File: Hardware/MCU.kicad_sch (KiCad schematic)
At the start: 27 parts, among them J6 USART Breakout, J7 SWD, SW1 Reset, U3 STM32L431CBTx, Y1 8M

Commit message: organization, updated submodule
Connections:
- net LED_FAULT: now reaches R13.1
- net LED_FAULT: now also U3.14 (PA4)
- net LED_CHARGE: now reaches R14.1
- net LED_CHARGE: now also U3.15 (PA5)
- net LED_DISCHARGE: now reaches R15.1
- net LED_DISCHARGE: now also U3.16 (PA6)
- net LED_HB: now reaches U3.13 (PA3)
- net LED_HB: now also R12.1
- net PA0 renamed ADC1_IN5
- net ADC1_IN5: no longer R12.1
- net PA1: no longer names the net of U3.11 (PA1)
- no-connect marks 27 -> 24
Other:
- note added: "LED Indicators"
- note removed: "Keep terminating resistors close to the pins Make sure to put resistor at MISO at the other end"
- note removed: "LEDs"
- moved on the sheet: C10, C11, C12, C7, C8, C9

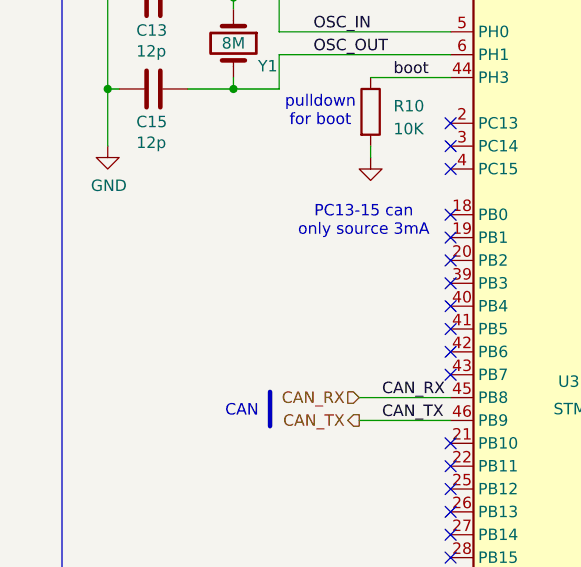
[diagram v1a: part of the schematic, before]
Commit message: new isolated amp, filter stage; need to select values
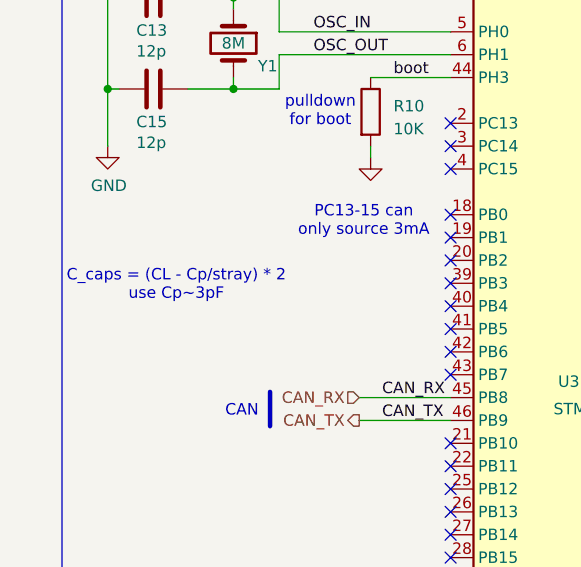
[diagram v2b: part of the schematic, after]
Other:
- note added: "C_caps = (CL - Cp/stray) * 2 use Cp~3pF"
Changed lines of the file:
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@@
+		)
+	)
+	(text "C_caps = (CL - Cp/stray) * 2\nuse Cp~3pF"
+		(exclude_from_sim no)
+		(at 27.94 68.834 0)
+		(effects
+			(font
+				(size 1.27 1.27)
+			)
 		)
 	)

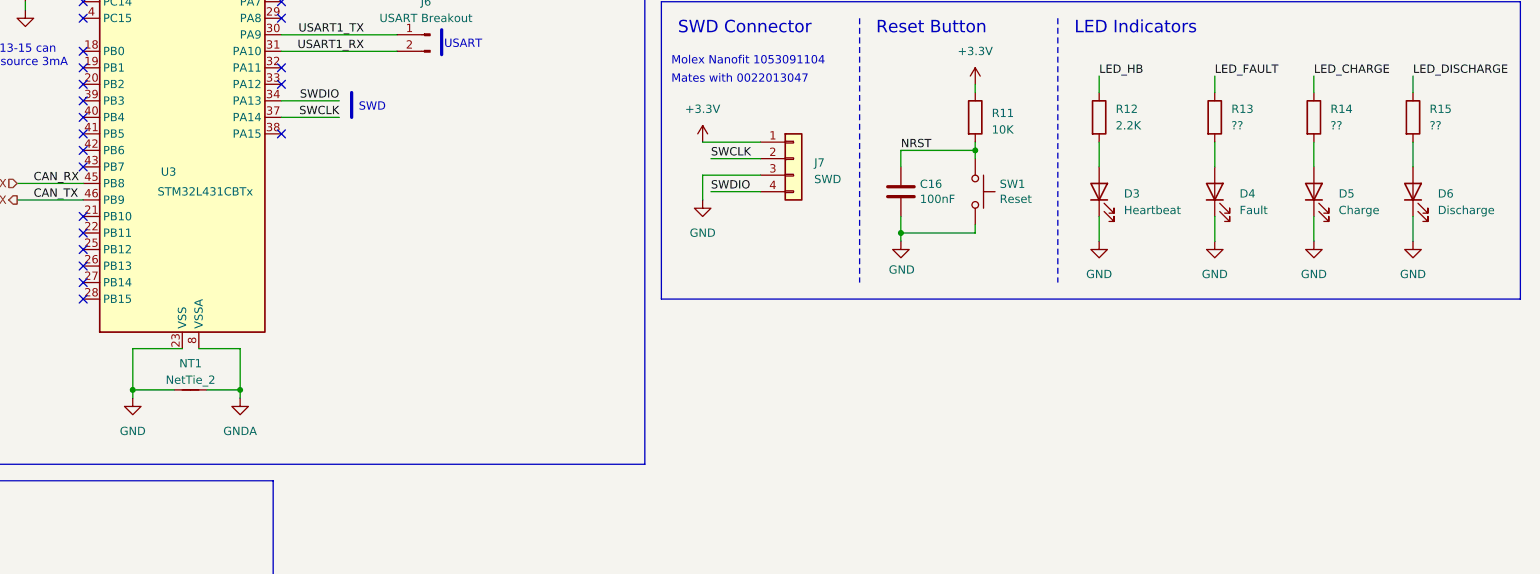
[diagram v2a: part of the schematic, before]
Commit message: added LEDs, changed LDO, still need to address other comments
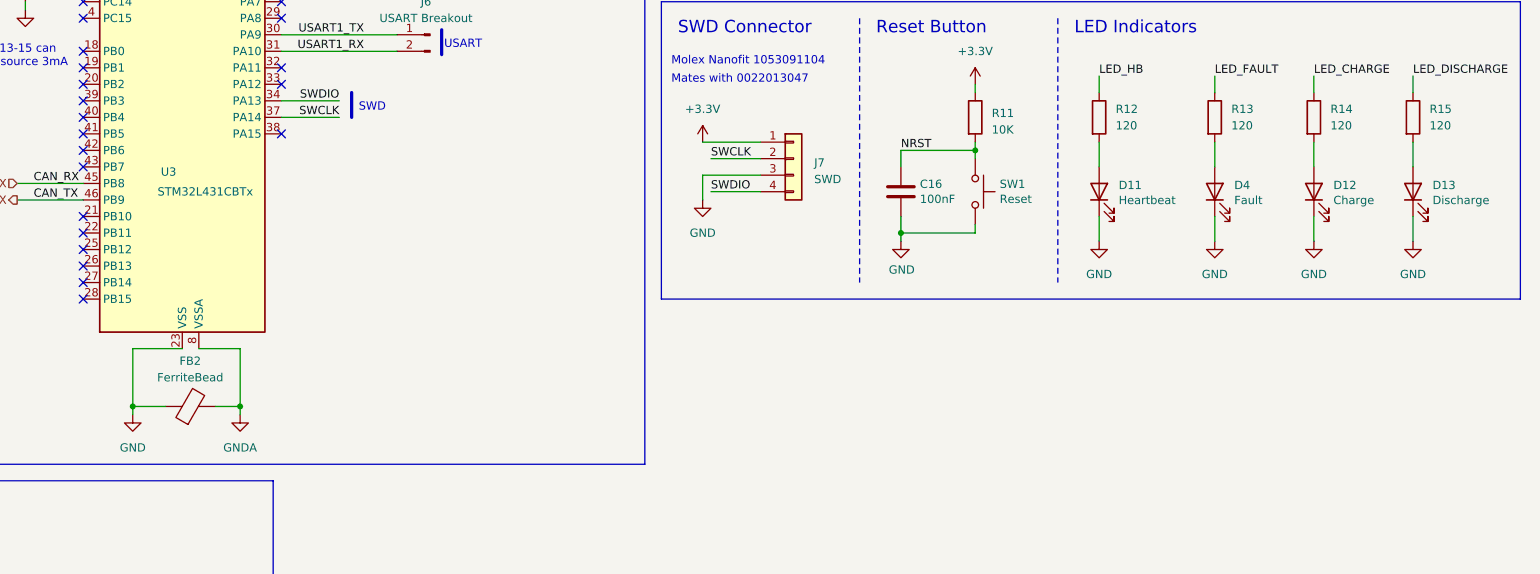
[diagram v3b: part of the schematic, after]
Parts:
- removed D3: Heartbeat, LED_SMD:LED_0805_2012Metric, symbol Device:LED
- removed D5: Charge, LED_SMD:LED_0805_2012Metric, symbol Device:LED
- removed D6: Discharge, LED_SMD:LED_0805_2012Metric, symbol Device:LED
- removed NT1: NetTie_2, NetTie:NetTie-2_SMD_Pad0.5mm, symbol Device:NetTie_2
- added D11: Heartbeat, symbol Device:LED
- added D12: Charge, symbol Device:LED
- added D13: Discharge, symbol Device:LED
- added FB2: FerriteBead, Inductor_SMD:L_0805_2012Metric, symbol Device:FerriteBead
- D4: footprint LED_SMD:LED_0805_2012Metric -> (none); Mfg (none) -> NCD0603R1
- R12: value 2.2K -> 120
- R13, R14, R15: value ?? -> 120
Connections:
- net GND: now also D11.1 (K), D12.1 (K), D13.1 (K), FB2.1
- net GNDA: now also FB2.2
- net at R14.2: now also D12.2 (A)
- net at R15.2: now also D13.2 (A)
- net at R12.2: now also D11.2 (A)

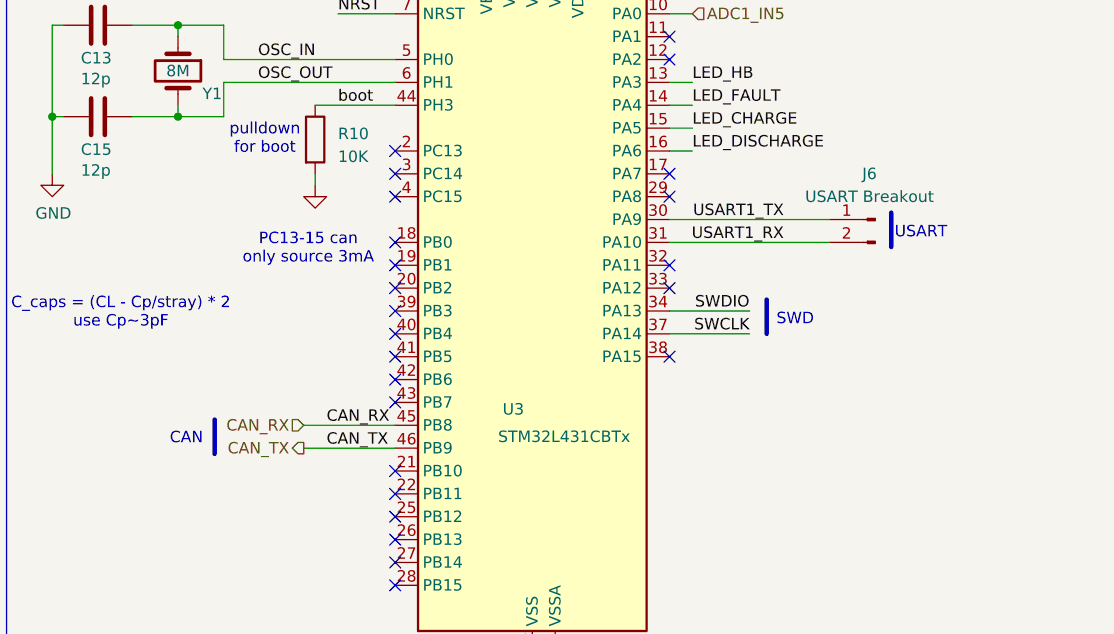
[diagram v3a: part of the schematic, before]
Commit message: scrutineering should be done, started on USB
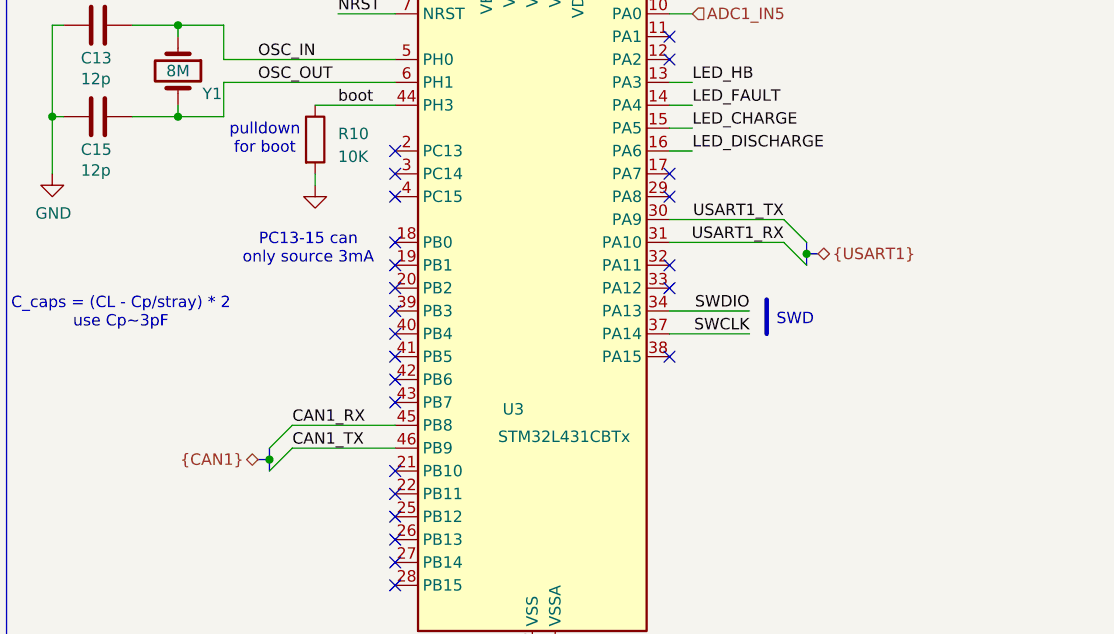
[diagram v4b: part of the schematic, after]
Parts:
- removed J6: USART Breakout, Connector_PinHeader_2.54mm:PinHeader_1x02_P2.54mm_Vertical, symbol Connector:Conn_01x02_Pin
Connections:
- net CAN_RX renamed CAN1_RX
- net CAN_TX renamed CAN1_TX
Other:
- note removed: "CAN"
- note removed: "USART"

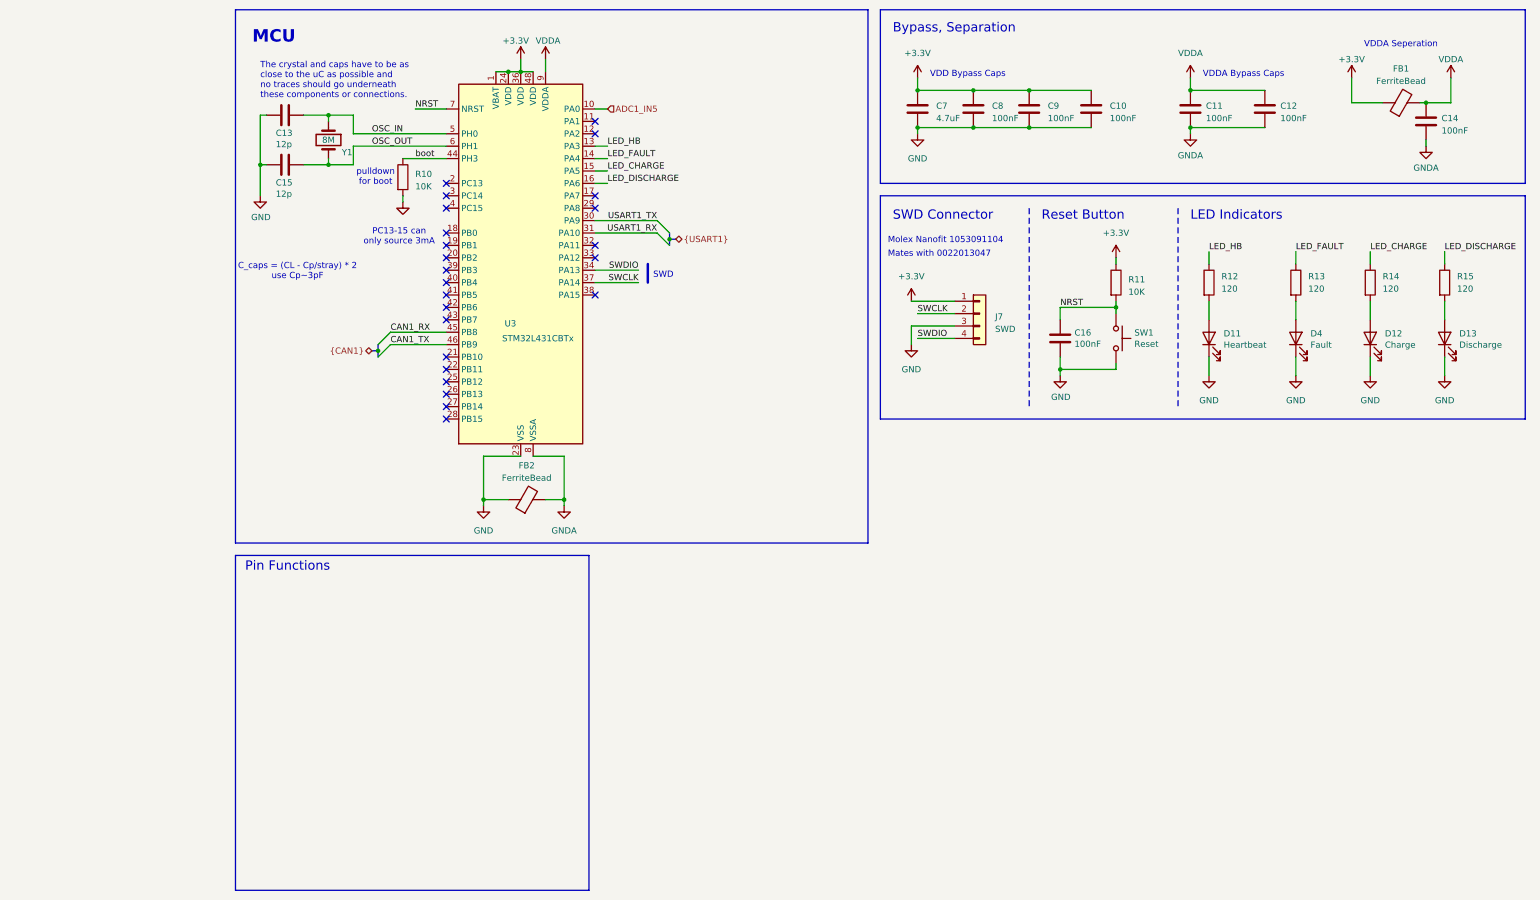
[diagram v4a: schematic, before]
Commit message: copied USB-C from psom
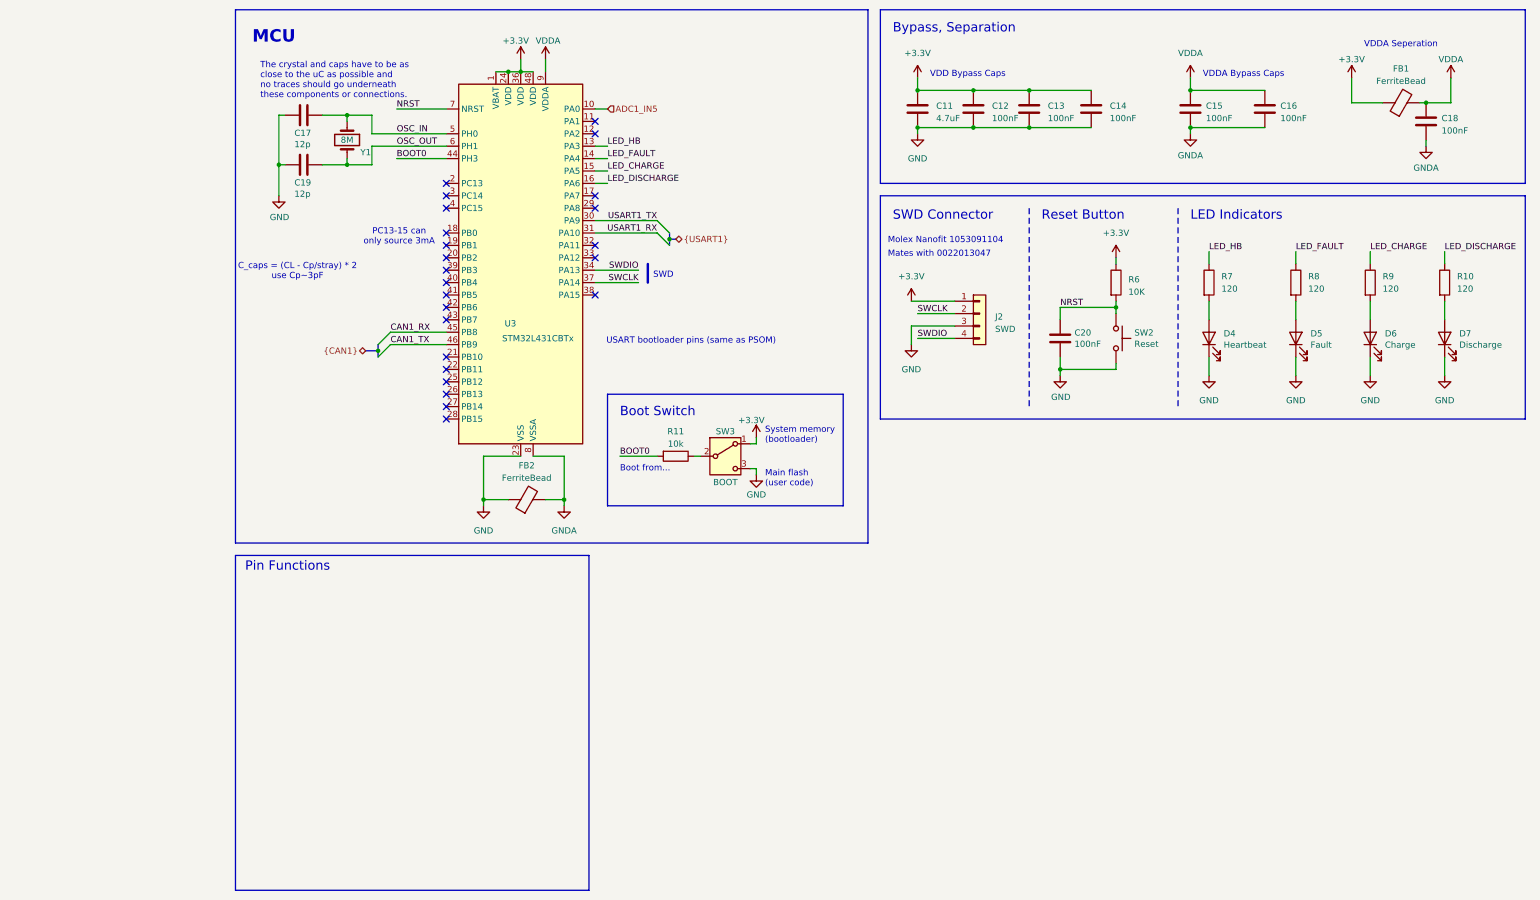
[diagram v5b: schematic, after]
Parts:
- removed R10: 10K, Resistor_SMD:R_0805_2012Metric, symbol Device:R
- added R11: 10k, Resistor_SMD:R_0603_1608Metric_Pad0.98x0.95mm_HandSolder, symbol Device:R
- added SW3: BOOT, CJS-1200TA:SW_CJS-1200TA, symbol Switch:SW_SPDT
- renumbered C7 to C11, C8 to C12, C9 to C13, C10 to C14, C11 to C15, C12 to C16, C13 to C17, C14 to C18, C15 to C19, C16 to C20, D11 to D4, D4 to D5, D12 to D6, D13 to D7, J7 to J2, R15 to R10, R11 to R6, R12 to R7, R13 to R8, R14 to R9, SW1 to SW2
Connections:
- net +3.3V: now also SW3.1 (A)
- net GND: now also SW3.3 (C)
- net boot renamed BOOT0
- net BOOT0: now also R11.2
- new net: R11.1, SW3.2 (B)
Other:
- note added: "Boot Switch"
- note added: "Boot from..."
- note added: "Main flash (user code)"
- note added: "System memory (bootloader)"
- note added: "USART bootloader pins (same as PSOM)"
- note removed: "pulldown for boot"
- moved on the sheet: C17, C19, Y1

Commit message: something changed idk what though
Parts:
- renumbered C11 to C18, C12 to C19, C13 to C20, C14 to C21, C15 to C22, C16 to C23, C17 to C24, C18 to C25, C19 to C26, C20 to C27, D4 to D6, D5 to D7, D6 to D8, D7 to D9, J2 to J3, R6 to R11, R7 to R12, R8 to R13, R9 to R14, R10 to R15, R11 to R16, U3 to U4

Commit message: 0603 footprints
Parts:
- C18, C19, C20, C21, C22, C23, C24, C25, C26, C27: footprint Capacitor_SMD:C_0805_2012Metric -> Capacitor_SMD:C_0603_1608Metric_Pad1.08x0.95mm_HandSolder
- D6, D7, D8, D9: footprint (none) -> LED_SMD:LED_0603_1608Metric_Pad1.05x0.95mm_HandSolder
- FB1, FB2: footprint Inductor_SMD:L_0805_2012Metric -> Capacitor_SMD:C_0603_1608Metric_Pad1.08x0.95mm_HandSolder
- R11, R12, R13, R14, R15: footprint Resistor_SMD:R_0805_2012Metric -> Resistor_SMD:R_0603_1608Metric_Pad0.98x0.95mm_HandSolder
- SW3: footprint CJS-1200TA:SW_CJS-1200TA -> Parts:SW_CJS-1200TA
- Y1: footprint Crystal:Crystal_SMD_TXC_7A-2Pin_5x3.2mm -> Crystal:Crystal_SMD_Abracon_ABM3-2Pin_5.0x3.2mm
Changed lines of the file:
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@@
 			)
 		)
-		(property "Footprint" "Capacitor_SMD:C_0805_2012Metric"
+		(property "Footprint" "Capacitor_SMD:C_0603_1608Metric_Pad1.08x0.95mm_HandSolder"
 			(at 185.1152 86.36 0)
 			(effects
@@
 			)
 		)
-		(property "Footprint" "Capacitor_SMD:C_0805_2012Metric"
+		(property "Footprint" "Capacitor_SMD:C_0603_1608Metric_Pad1.08x0.95mm_HandSolder"
 			(at 260.0452 41.91 0)
 			(effects
@@
 			)
 		)
-		(property "Footprint" "Capacitor_SMD:C_0805_2012Metric"
+		(property "Footprint" "Capacitor_SMD:C_0603_1608Metric_Pad1.08x0.95mm_HandSolder"
 			(at 191.4652 39.37 0)
 			(effects
@@
 			)
 		)
-		(property "Footprint" "Inductor_SMD:L_0805_2012Metric"
+		(property "Footprint" "Capacitor_SMD:C_0603_1608Metric_Pad1.08x0.95mm_HandSolder"
 			(at 254 36.068 90)
 			(effects
@@
 			)
 		)
-		(property "Footprint" ""
+		(property "Footprint" "LED_SMD:LED_0603_1608Metric_Pad1.05x0.95mm_HandSolder"
 			(at 232.41 82.55 0)
 			(effects
@@
 			)
 		)
-		(property "Footprint" ""
+		(property "Footprint" "LED_SMD:LED_0603_1608Metric_Pad1.05x0.95mm_HandSolder"
 			(at 214.63 82.55 0)
 			(effects
@@
 			)
 		)
-		(property "Footprint" "Resistor_SMD:R_0805_2012Metric"
+		(property "Footprint" "Resistor_SMD:R_0603_1608Metric_Pad0.98x0.95mm_HandSolder"
 			(at 230.632 71.12 90)
 			(effects
@@
 			)
 		)
-		(property "Footprint" "Capacitor_SMD:C_0805_2012Metric"
+		(property "Footprint" "Capacitor_SMD:C_0603_1608Metric_Pad1.08x0.95mm_HandSolder"
 			(at 25.4 47.9552 0)
 			(effects
@@
 			)
 		)
-		(property "Footprint" "CJS-1200TA:SW_CJS-1200TA"
+		(property "Footprint" "Parts:SW_CJS-1200TA"
 			(at 115.57 106.68 0)
 			(effects
@@
 			)
 		)
-		(property "Footprint" "Capacitor_SMD:C_0805_2012Metric"
+		(property "Footprint" "Capacitor_SMD:C_0603_1608Metric_Pad1.08x0.95mm_HandSolder"
 			(at 211.7852 39.37 0)
 			(effects
@@
 			)
 		)
-		(property "Footprint" ""
+		(property "Footprint" "LED_SMD:LED_0603_1608Metric_Pad1.05x0.95mm_HandSolder"
 			(at 247.65 82.55 0)
 			(effects
@@
 			)
 		)
-		(property "Footprint" "Resistor_SMD:R_0805_2012Metric"
+		(property "Footprint" "Resistor_SMD:R_0603_1608Metric_Pad0.98x0.95mm_HandSolder"
 			(at 245.872 71.12 90)
 			(effects
@@
 			)
 		)
-		(property "Footprint" "Capacitor_SMD:C_0805_2012Metric"
+		(property "Footprint" "Capacitor_SMD:C_0603_1608Metric_Pad1.08x0.95mm_HandSolder"
 			(at 167.3352 39.37 0)
 			(effects
@@
 			)
 		)
-		(property "Footprint" "Resistor_SMD:R_0805_2012Metric"
+		(property "Footprint" "Resistor_SMD:R_0603_1608Metric_Pad0.98x0.95mm_HandSolder"
 			(at 261.112 71.12 90)
 			(effects
@@
 			)
 		)
-		(property "Footprint" ""
+		(property "Footprint" "LED_SMD:LED_0603_1608Metric_Pad1.05x0.95mm_HandSolder"
 			(at 262.89 82.55 0)
 			(effects
@@
 			)
 		)
-		(property "Footprint" "Crystal:Crystal_SMD_TXC_7A-2Pin_5x3.2mm"
+		(property "Footprint" "Crystal:Crystal_SMD_Abracon_ABM3-2Pin_5.0x3.2mm"
 			(at 38.1 41.91 0)
 			(effects
@@
 			)
 		)
-		(property "Footprint" "Capacitor_SMD:C_0805_2012Metric"
+		(property "Footprint" "Capacitor_SMD:C_0603_1608Metric_Pad1.08x0.95mm_HandSolder"
 			(at 227.0252 39.37 0)
 			(effects
@@
 			)
 		)
-		(property "Footprint" "Capacitor_SMD:C_0805_2012Metric"
+		(property "Footprint" "Capacitor_SMD:C_0603_1608Metric_Pad1.08x0.95mm_HandSolder"
 			(at 155.9052 39.37 0)
 			(effects
@@
 			)
 		)
-		(property "Footprint" "Resistor_SMD:R_0805_2012Metric"
+		(property "Footprint" "Resistor_SMD:R_0603_1608Metric_Pad0.98x0.95mm_HandSolder"
 			(at 212.852 71.12 90)
 			(effects
@@
 			)
 		)
-		(property "Footprint" "Resistor_SMD:R_0805_2012Metric"
+		(property "Footprint" "Resistor_SMD:R_0603_1608Metric_Pad0.98x0.95mm_HandSolder"
 			(at 193.802 71.12 90)
 			(effects
@@
 			)
 		)
-		(property "Footprint" "Capacitor_SMD:C_0805_2012Metric"
+		(property "Footprint" "Capacitor_SMD:C_0603_1608Metric_Pad1.08x0.95mm_HandSolder"
 			(at 178.7652 39.37 0)
 			(effects
@@
 			)
 		)
-		(property "Footprint" "Capacitor_SMD:C_0805_2012Metric"
+		(property "Footprint" "Capacitor_SMD:C_0603_1608Metric_Pad1.08x0.95mm_HandSolder"
 			(at 25.4 37.7952 0)
 			(effects
@@
 			)
 		)
-		(property "Footprint" "Inductor_SMD:L_0805_2012Metric"
+		(property "Footprint" "Capacitor_SMD:C_0603_1608Metric_Pad1.08x0.95mm_HandSolder"
 			(at 74.93 117.348 90)
 			(effects
